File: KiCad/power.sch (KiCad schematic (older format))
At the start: 6 parts, among them J11 PSU_CTRL, J12 POWER

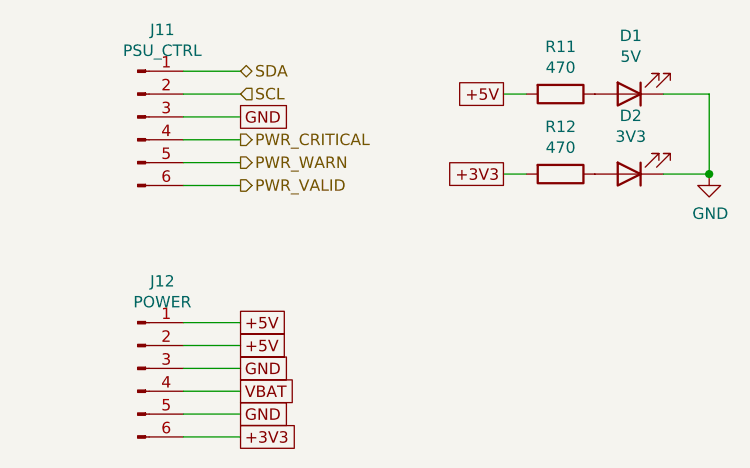
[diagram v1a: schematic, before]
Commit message: Change all SH connectors to horizontal
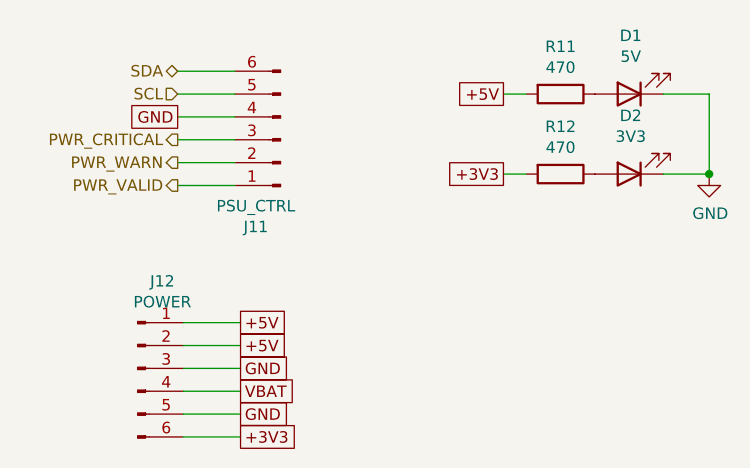
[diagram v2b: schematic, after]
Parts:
- J11: footprint Connector_JST:JST_SH_BM06B-SRSS-TB_1x06-1MP_P1.00mm_Vertical -> Connector_JST:JST_SH_SM06B-SRSS-TB_1x06-1MP_P1.00mm_Horizontal
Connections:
- net GND: now also J11.4 (Pin_4); no longer J11.3 (Pin_3)
- net PWR_CRITICAL: now also J11.3 (Pin_3); no longer J11.4 (Pin_4)
- net PWR_VALID: now also J11.1 (Pin_1); no longer J11.6 (Pin_6)
- net PWR_WARN: now also J11.2 (Pin_2); no longer J11.5 (Pin_5)
- net SCL: now also J11.5 (Pin_5); no longer J11.2 (Pin_2)
- net SDA: now also J11.6 (Pin_6); no longer J11.1 (Pin_1)
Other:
- moved on the sheet: J11
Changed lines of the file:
@@
 	1600 2250 1350 2250
 Wire Wire Line
-	1600 1150 1350 1150
-Text HLabel 1600 1650 2    50   Output ~ 0
+	1575 1150 1325 1150
+Text HLabel 1325 1650 0    50   Output ~ 0
 PWR_VALID
-Text HLabel 1600 1550 2    50   Output ~ 0
+Text HLabel 1325 1550 0    50   Output ~ 0
 PWR_WARN
-Text HLabel 1600 1450 2    50   Output ~ 0
+Text HLabel 1325 1450 0    50   Output ~ 0
 PWR_CRITICAL
-$Comp
-L Connector:Conn_01x06_Male J11
-U 1 1 5FCAB8A7
-P 1150 1350
-F 0 "J11" H 1258 1731 50  0000 C CNN
-F 1 "PSU_CTRL" H 1258 1640 50  0000 C CNN
-F 2 "Connector_JST:JST_SH_BM06B-SRSS-TB_1x06-1MP_P1.00mm_Vertical" H 1150 1350 50  0001 C CNN
-F 3 "~" H 1150 1350 50  0001 C CNN
-	1    1150 1350
-	1    0    0    -1
-$EndComp
-Text GLabel 1600 1350 2    50   UnSpc ~ 0
+Text GLabel 1325 1350 0    50   UnSpc ~ 0
 GND
-Text HLabel 1600 1250 2    50   Input ~ 0
+Text HLabel 1325 1250 0    50   Input ~ 0
 SCL
-Text HLabel 1600 1150 2    50   BiDi ~ 0
+Text HLabel 1325 1150 0    50   BiDi ~ 0
 SDA
 Wire Wire Line
-	1600 1650 1350 1650
+	1575 1650 1325 1650
 Wire Wire Line
-	1600 1550 1350 1550
+	1575 1550 1325 1550
 Wire Wire Line
-	1600 1450 1350 1450
+	1575 1450 1325 1450
 Wire Wire Line
-	1600 1350 1350 1350
+	1575 1350 1325 1350
 Wire Wire Line
-	1600 1250 1350 1250
+	1575 1250 1325 1250
 $Comp
 L Connector:Conn_01x06_Male J12
@@
 	1    0    0    -1
 $EndComp
+$Comp
+L Connector:Conn_01x06_Male J11
+U 1 1 5FCAB8A7
+P 1775 1450
+F 0 "J11" H 1883 1831 50  0000 C CNN
+F 1 "PSU_CTRL" H 1883 1740 50  0000 C CNN
+F 2 "Connector_JST:JST_SH_SM06B-SRSS-TB_1x06-1MP_P1.00mm_Horizontal" H 1775 1450 50  0001 C CNN
+F 3 "~" H 1775 1450 50  0001 C CNN
+	1    1775 1450
+	-1   0    0    1
+$EndComp
 $EndSCHEMATC
